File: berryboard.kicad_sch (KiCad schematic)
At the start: 42 parts, among them J1 XT30_SERVO_PWR, J12 QWIIC_RPI_1, J13 QWIIC_RPI_2, J14 QWIIC_RPI_3, J15 QWIIC_MCU_1, J16 QWIIC_MCU_2, J17 QWIIC_MCU_3, J18 LEAK_1, J19 LEAK_2, J2 RPi_GPIO_40P, J20 HAT_5V_IN, J21 SWD, J3 USB_C_RP2350, J4 SERVO_SIG, J5 SERVO_PWR, J6 SERVO_GND, U1 TPS2121, U2 AP2112K-3.3, U3 ICM-42688-P, U4 MMC5983MA, U5 24LC32, U6 RP2350B, U7 W25Q16JVSS

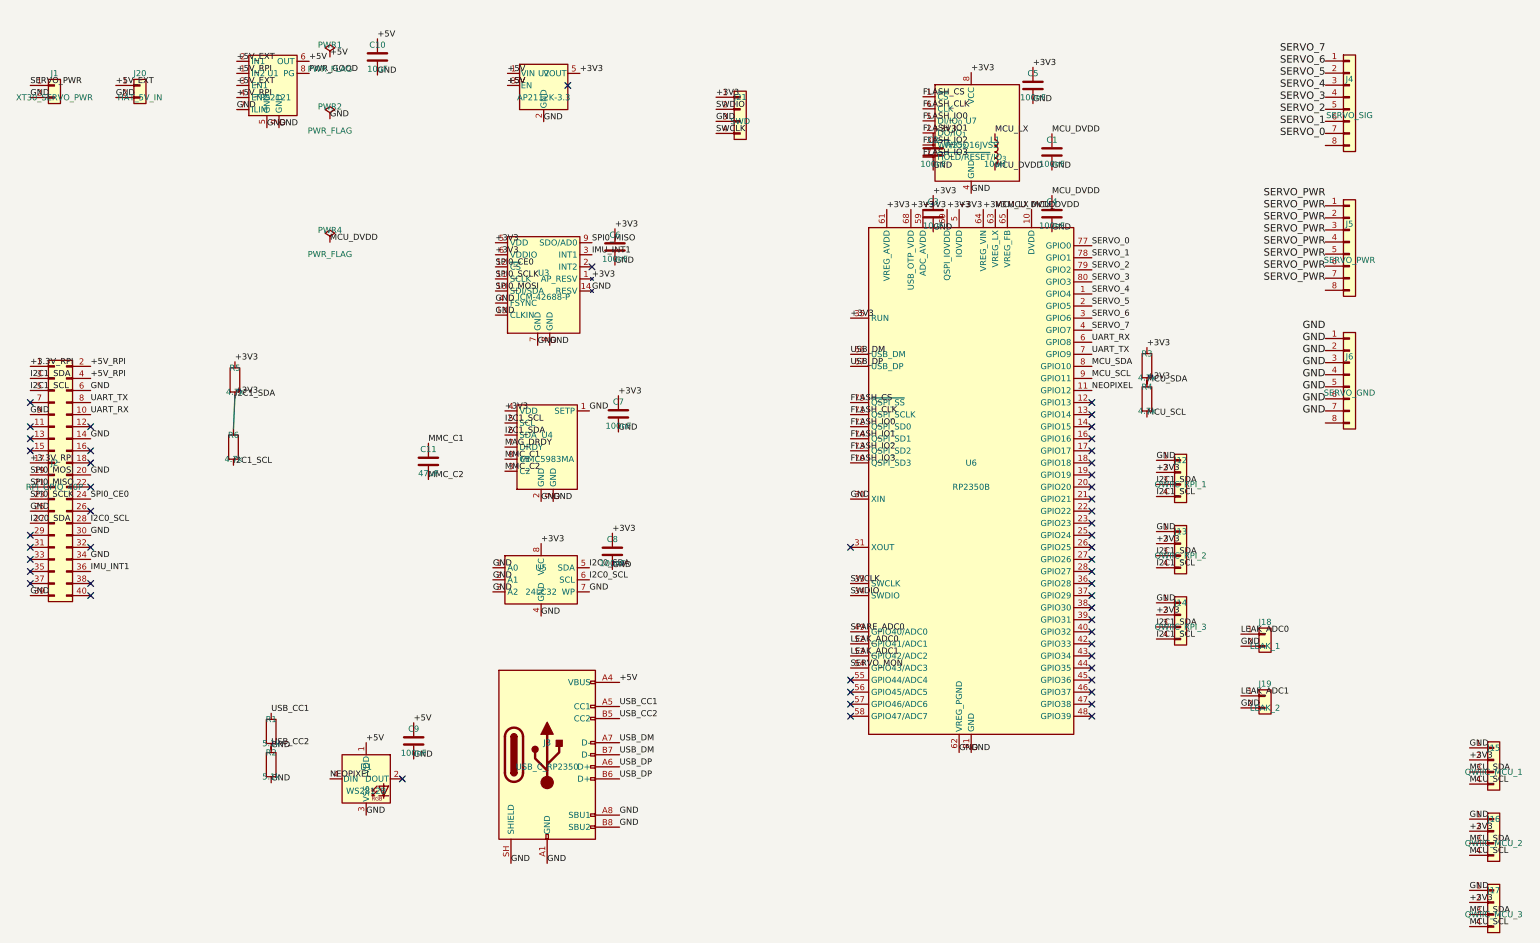
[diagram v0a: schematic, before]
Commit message: PCB: fix servo header spacing and order; schematic: add SERVO_PWR protection and SERVO_MON divider
PCB changes:
- Reorder J4/J5/J6 so signal (J4) is at top (y=77.5), power (J5) at y=80.04,
  ground (J6) at y=82.58 — matches yellow/red/black color convention
- Fix row spacing to exactly 2.54mm so a 3-pin Dupont housing mates all three
  rows simultaneously
- Align all three X coordinates to 143.22
- Add F.SilkS channel labels "1"–"8" above the servo header block

Schematic changes:
- Add D2 (SMBJ7.5A TVS diode) from SERVO_PWR to GND for transient protection
- Add C12 (100µF bulk capacitor) on SERVO_PWR for servo current decoupling
- Add R7/R8 (220k/100k) voltage divider: SERVO_PWR → SERVO_MON → GND,
  scaling up to 8.4V battery down to ≤2.6V for RP2350B ADC3 input
- U4 (MMC5983MA) footprint confirmed correct: OptoDevice:Broadcom_LGA-8_2x2mm_P0.5mm
  is the only matching 2×2mm / 0.5mm pitch LGA-8 in KiCad standard library
- U5 (24LC32) DNP flag confirmed already clear

Co-Authored-By: Claude Sonnet 4.6 <noreply@anthropic.com>
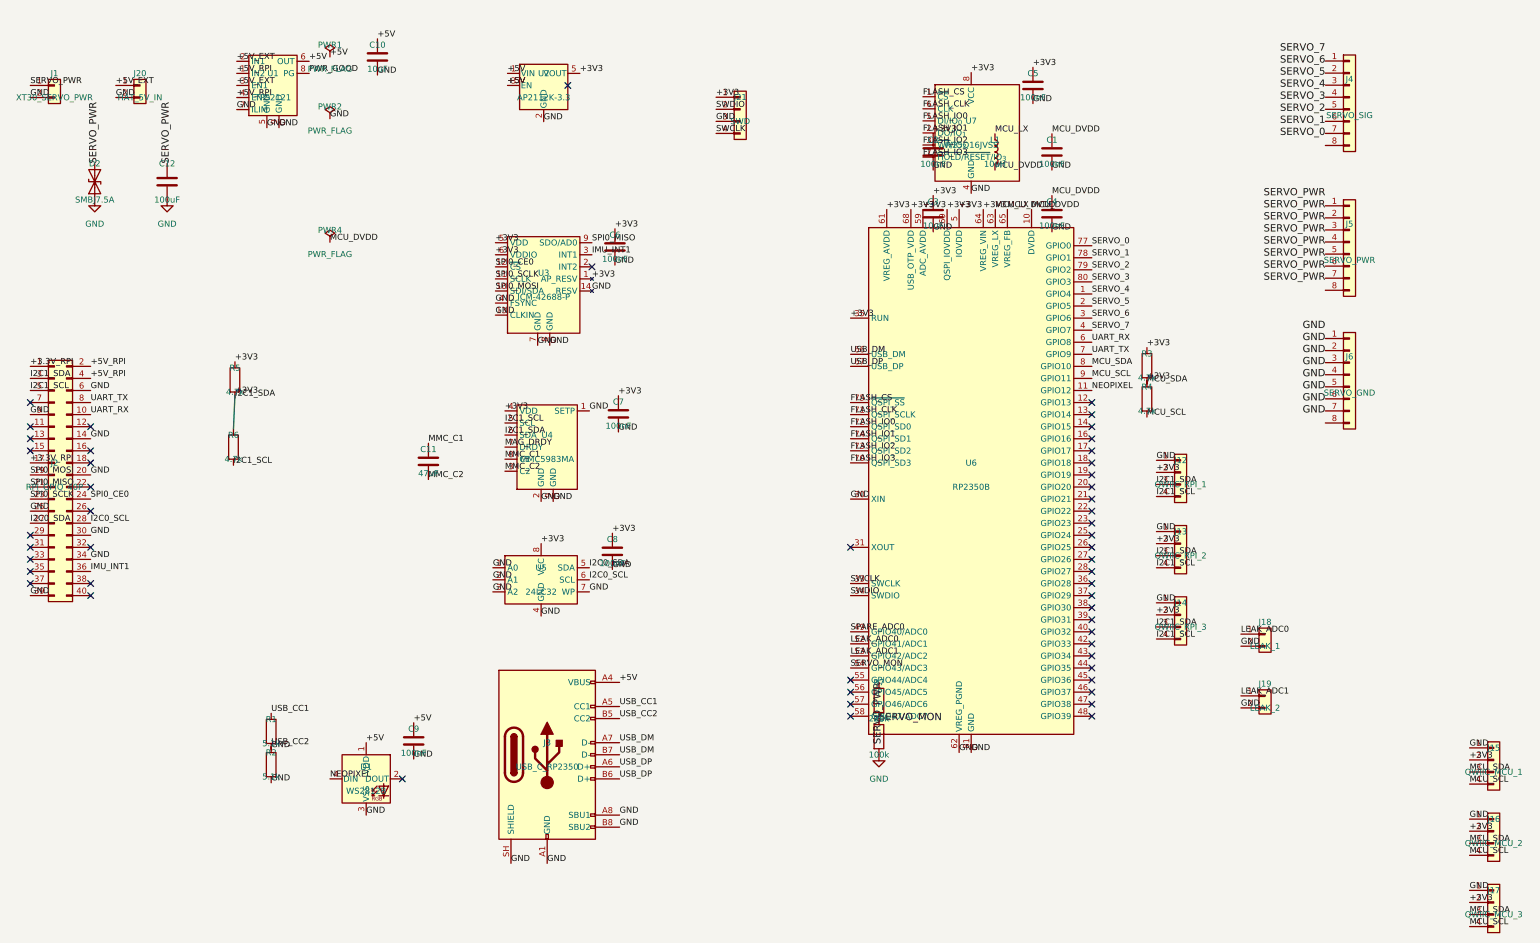
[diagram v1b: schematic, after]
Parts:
- added C12: 100uF, Capacitor_SMD:C_1206_3216Metric, symbol Device:C
- added D2: SMBJ7.5A, Diode_SMD:D_SMB, symbol Device:D_TVS
- added R7: 220k, Resistor_SMD:R_0402_1005Metric, symbol Device:R
- added R8: 100k, Resistor_SMD:R_0402_1005Metric, symbol Device:R
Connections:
- net GND: now also C12.2, D2.1 (A1), R8.2
- net SERVO_MON: now also R7.2, R8.1
- net SERVO_PWR: now also C12.1, D2.2 (A2), R7.1
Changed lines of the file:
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@@
 		(effects (font (size 1.524 1.524)))
+	)
+	(symbol
+		(lib_id "Device:D_TVS")
+		(at 30.48 48.26 90)
+		(unit 1)
+		(exclude_from_sim no)
+		(in_bom yes)
+		(on_board yes)
+		(dnp no)
+		(property "Reference" "D2"
+			(at 30.48 44.45 90)
+			(effects (font (size 1.27 1.27)))
+		)
+		(property "Value" "SMBJ7.5A"
+			(at 30.48 52.07 90)
+			(effects (font (size 1.27 1.27)))
+		)
+		(property "Footprint" "Diode_SMD:D_SMB"
+			(at 30.48 48.26 90)
+			(effects (font (size 1.27 1.27)) (hide yes))
+		)
+		(property "Datasheet" "~"
+			(at 30.48 48.26 0)
+			(effects (font (size 1.27 1.27)) (hide yes))
+		)
+		(instances
+			(project "berryboard"
+				(path "/8a84b133-444f-4bc0-8559-a8dc66e5a739"
+					(reference "D2") (unit 1)
+				)
+			)
+		)
+	)
+	(symbol
+		(lib_id "Device:C")
+		(at 45.72 48.26 0)
+		(unit 1)
+		(exclude_from_sim no)
+		(in_bom yes)
+		(on_board yes)
+		(dnp no)
+		(property "Reference" "C12"
+			(at 45.72 44.45 0)
+			(effects (font (size 1.27 1.27)))
+		)
+		(property "Value" "100uF"
+			(at 45.72 52.07 0)
+			(effects (font (size 1.27 1.27)))
+		)
+		(property "Footprint" "Capacitor_SMD:C_1206_3216Metric"
+			(at 45.72 48.26 0)
+			(effects (font (size 1.27 1.27)) (hide yes))
+		)
+		(property "Datasheet" "~"
+			(at 45.72 48.26 0)
+			(effects (font (size 1.27 1.27)) (hide yes))
+		)
+		(instances
+			(project "berryboard"
+				(path "/e14f9120-b985-4aa8-baee-3d97ad23c394"
+					(reference "C12") (unit 1)
+				)
+			)
+		)
+	)
+	(symbol
+		(lib_id "Device:R")
+		(at 195.58 157.48 0)
+		(unit 1)
+		(exclude_from_sim no)
+		(in_bom yes)
+		(on_board yes)
+		(dnp no)
+		(property "Reference" "R7"
+			(at 195.58 153.67 0)
+			(effects (font (size 1.27 1.27)))
+		)
+		(property "Value" "220k"
+			(at 195.58 161.29 0)
+			(effects (font (size 1.27 1.27)))
+		)
+		(property "Footprint" "Resistor_SMD:R_0402_1005Metric"
+			(at 195.58 157.48 0)
+			(effects (font (size 1.27 1.27)) (hide yes))
+		)
+		(property "Datasheet" "~"
+			(at 195.58 157.48 0)
+			(effects (font (size 1.27 1.27)) (hide yes))
+		)
+		(instances
+			(project "berryboard"
+				(path "/37db72fe-720e-4c7e-8a5f-5282c0f2cdd9"
+					(reference "R7") (unit 1)
+				)
+			)
+		)
+	)
+	(symbol
+		(lib_id "Device:R")
+		(at 195.58 165.1 0)
+		(unit 1)
+		(exclude_from_sim no)
+		(in_bom yes)
+		(on_board yes)
+		(dnp no)
+		(property "Reference" "R8"
+			(at 195.58 161.29 0)
+			(effects (font (size 1.27 1.27)))
+		)
+		(property "Value" "100k"
+			(at 195.58 168.91 0)
+			(effects (font (size 1.27 1.27)))
+		)
+		(property "Footprint" "Resistor_SMD:R_0402_1005Metric"
+			(at 195.58 165.1 0)
+			(effects (font (size 1.27 1.27)) (hide yes))
+		)
+		(property "Datasheet" "~"
+			(at 195.58 165.1 0)
+			(effects (font (size 1.27 1.27)) (hide yes))
+		)
+		(instances
+			(project "berryboard"
+				(path "/3ea6d4ef-2be0-4b57-a26a-e90b8120648b"
+					(reference "R8") (unit 1)
+				)
+			)
+		)
+	)
+	(label "SERVO_PWR"
+		(at 30.48 44.45 90)
+		(effects (font (size 1.524 1.524)))
+	)
+	(symbol
+		(lib_id "power:GND")
+		(at 30.48 52.07 0)
+		(unit 1)
+		(exclude_from_sim no)
+		(in_bom yes)
+		(on_board yes)
+		(dnp no)
+		(property "Reference" "#PWR0ccc"
+			(at 30.48 58.42 0)
+			(effects (font (size 1.27 1.27)) (hide yes))
+		)
+		(property "Value" "GND"
+			(at 30.48 57.15 0)
+			(effects (font (size 1.27 1.27)))
+		)
+		(property "Footprint" ""
+			(at 30.48 52.07 0)
+			(effects (font (size 1.27 1.27)) (hide yes))
+		)
+		(property "Datasheet" "~"
+			(at 30.48 52.07 0)
+			(effects (font (size 1.27 1.27)) (hide yes))
+		)
+		(instances
+			(project "berryboard"
+				(path "/a77e4e7f-d60c-4832-b8f3-bf3b153152f1"
+					(reference "#PWR0ccc") (unit 1)
+				)
+			)
+		)
+	)
+	(label "SERVO_PWR"
+		(at 45.72 44.45 90)
+		(effects (font (size 1.524 1.524)))
+	)
+	(symbol
+		(lib_id "power:GND")
+		(at 45.72 52.07 0)
+		(unit 1)
+		(exclude_from_sim no)
+		(in_bom yes)
+		(on_board yes)
+		(dnp no)
+		(property "Reference" "#PWRc61f"
+			(at 45.72 58.42 0)
+			(effects (font (size 1.27 1.27)) (hide yes))
+		)
+		(property "Value" "GND"
+			(at 45.72 57.15 0)
+			(effects (font (size 1.27 1.27)))
+		)
+		(property "Footprint" ""
+			(at 45.72 52.07 0)
+			(effects (font (size 1.27 1.27)) (hide yes))
+		)
+		(property "Datasheet" "~"
+			(at 45.72 52.07 0)
+			(effects (font (size 1.27 1.27)) (hide yes))
+		)
+		(instances
+			(project "berryboard"
+				(path "/cc1cd4d7-8d83-453a-a71e-830c8548b65a"
+					(reference "#PWRc61f") (unit 1)
+				)
+			)
+		)
+	)
+	(label "SERVO_PWR"
+		(at 195.58 153.67 270)
+		(effects (font (size 1.524 1.524)))
+	)
+	(label "SERVO_MON"
+		(at 195.58 161.29 0)
+		(effects (font (size 1.524 1.524)))
+	)
+	(symbol
+		(lib_id "power:GND")
+		(at 195.58 168.91 0)
+		(unit 1)
+		(exclude_from_sim no)
+		(in_bom yes)
+		(on_board yes)
+		(dnp no)
+		(property "Reference" "#PWR6d11"
+			(at 195.58 175.26 0)
+			(effects (font (size 1.27 1.27)) (hide yes))
+		)
+		(property "Value" "GND"
+			(at 195.58 173.99 0)
+			(effects (font (size 1.27 1.27)))
+		)
+		(property "Footprint" ""
+			(at 195.58 168.91 0)
+			(effects (font (size 1.27 1.27)) (hide yes))
+		)
+		(property "Datasheet" "~"
+			(at 195.58 168.91 0)
+			(effects (font (size 1.27 1.27)) (hide yes))
+		)
+		(instances
+			(project "berryboard"
+				(path "/d35c00af-0467-44ea-b31d-212ccfa49abc"
+					(reference "#PWR6d11") (unit 1)
+				)
+			)
+		)
 	)
 	(wire

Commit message: Connector footprint updates: female GPIO socket, vertical QWIIC
J2 (RPi 40-pin GPIO header):
- Footprint: PinHeader_2x20_P2.54mm_Vertical → PinSocket_2x20_P2.54mm_Vertical
- PCB layer: F.Cu → B.Cu (female socket on bottom of board to mate with RPi)
- All F.SilkS/F.Fab/F.CrtYd references flipped to B.* within the footprint block

J12–J17 (six QWIIC/JST-SH connectors):
- Footprint: JST_SH_SM04B-SRSS-TB_1x04-1MP_P1.00mm_Horizontal →
            JST_SH_BM04B-SRSS-TB_1x04-1MP_P1.00mm_Vertical
- Changed in both schematic and PCB

Co-Authored-By: Claude Sonnet 4.6 <noreply@anthropic.com>
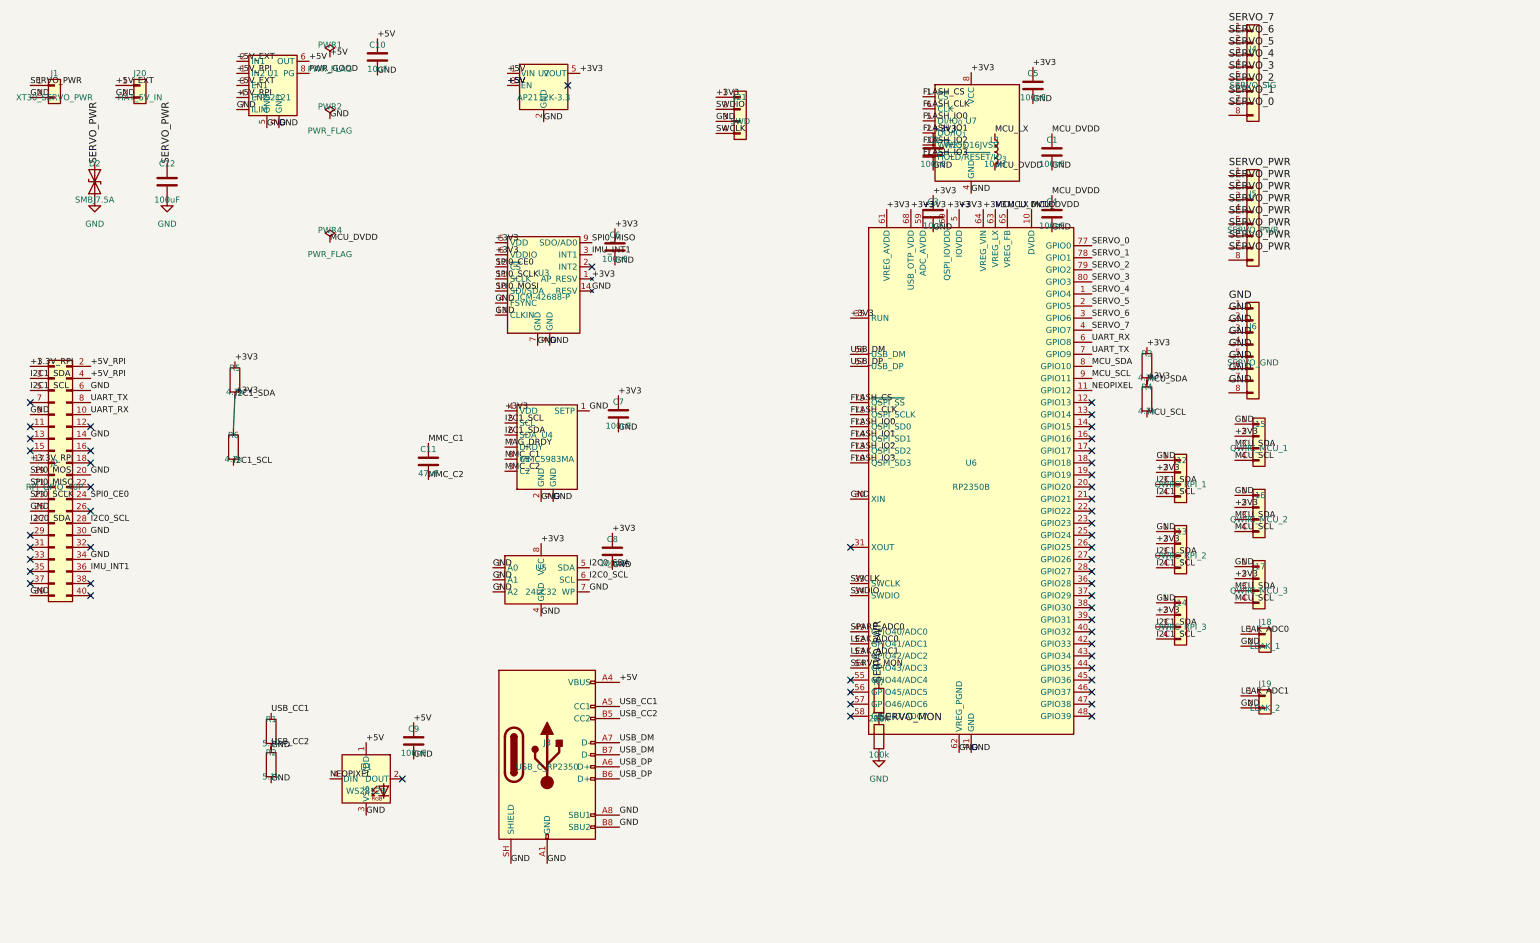
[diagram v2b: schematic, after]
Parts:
- J12, J13, J14, J15, J16, J17: footprint Connector_JST:JST_SH_SM04B-SRSS-TB_1x04-1MP_P1.00mm_Horizontal -> Connector_JST:JST_SH_BM04B-SRSS-TB_1x04-1MP_P1.00mm_Vertical
- J2: footprint Connector_PinHeader_2.54mm:PinHeader_2x20_P2.54mm_Vertical -> Connector_PinSocket_2.54mm:PinSocket_2x20_P2.54mm_Vertical
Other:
- moved on the sheet: J15, J16, J17, J4, J5, J6
